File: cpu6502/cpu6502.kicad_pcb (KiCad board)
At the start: 2 copper layers, 140 x 100 mm, 34 parts, among them J1 Conn_01x02, J2 Conn_02x05_Odd_Even, J3 Conn_02x21_Odd_Even, U1 74LS161, U2 W65C02SxP / MC6802 / R6502, U3 74LS573, U4 74LS573, U5 74LS573, U6 74LS245, U7 ATF22V10C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

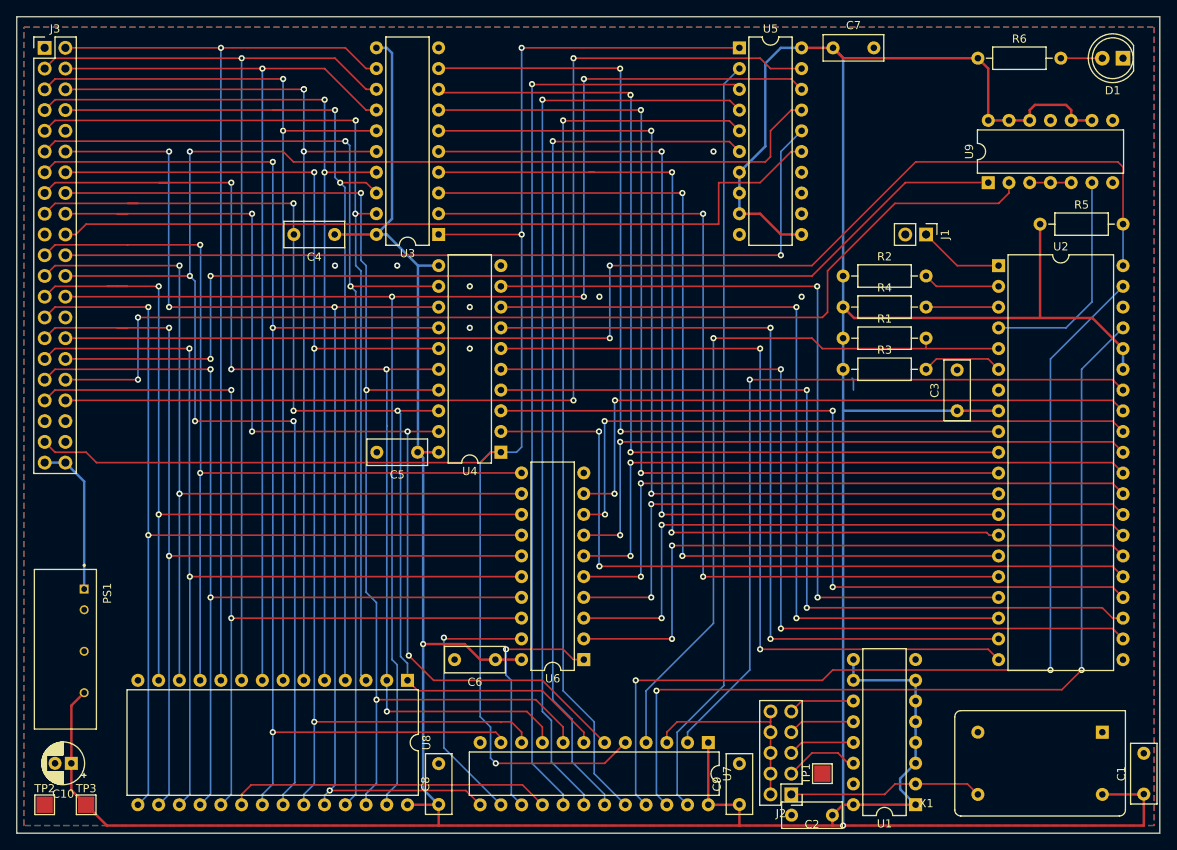
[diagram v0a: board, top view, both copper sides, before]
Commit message: Moved devices around and size reduced board.
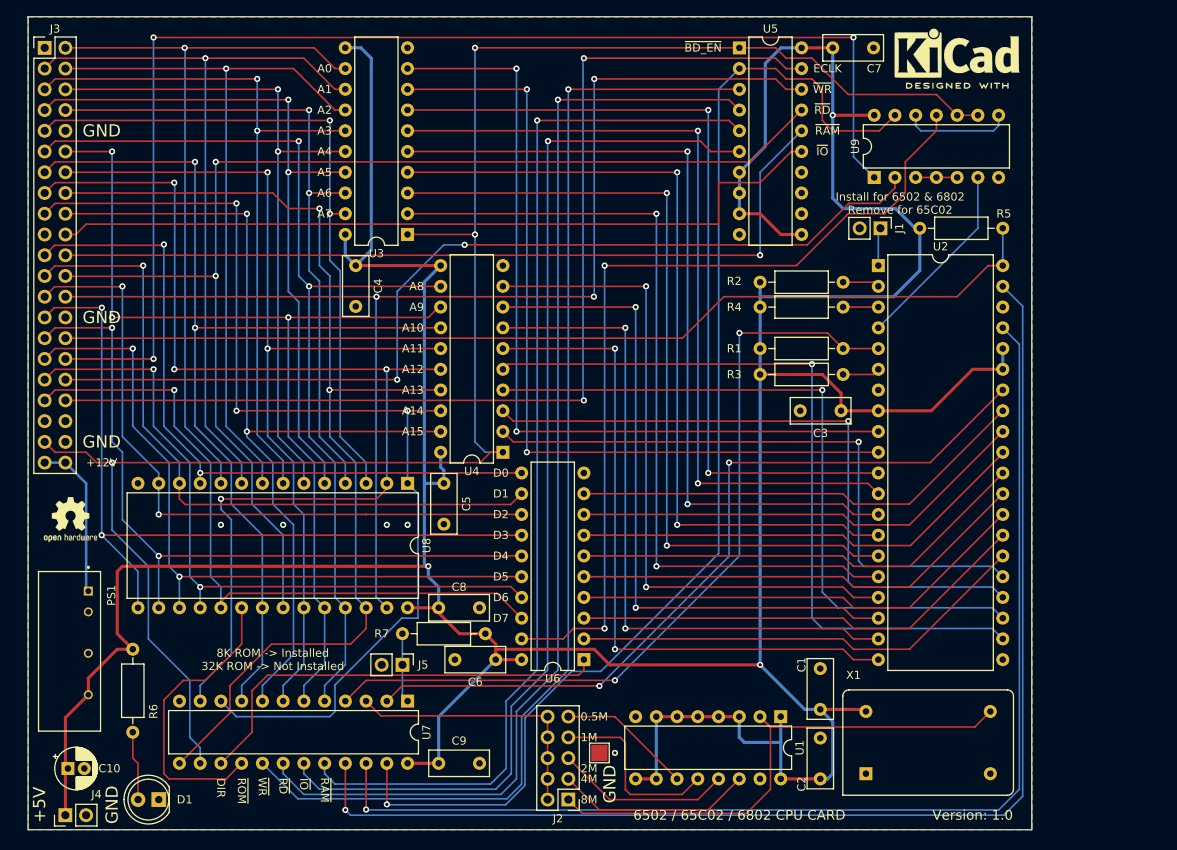
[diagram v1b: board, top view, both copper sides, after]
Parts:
- removed TP2, TP3: TestPoint, TestPoint:TestPoint_Pad_2.0x2.0mm
- added J4: Conn_01x02, Connector_PinHeader_2.54mm:PinHeader_1x02_P2.54mm_Vertical, F.Cu at (61.0, 148.6)
- added J5: Conn_01x02, Connector_PinHeader_2.54mm:PinHeader_1x02_P2.54mm_Vertical, F.Cu at (102.2, 130.2)
- added R7: 10.5K, Resistor_THT:R_Axial_DIN0207_L6.3mm_D2.5mm_P10.16mm_Horizontal, F.Cu at (102.2, 126.4)
- added REF**: OSHW-Logo2_7.3x6mm_SilkScreen, Symbol:OSHW-Logo2_7.3x6mm_SilkScreen, F.Cu at (61.6, 112.4)
- added REF**: KiCad-Logo2_6mm_SilkScreen, Symbol:KiCad-Logo2_6mm_SilkScreen, F.Cu at (170.2, 55.2)
- moved D1 149.0 mm to (72.4, 146.7)
- moved R6 126.3 mm to (69.2, 128.3), turned to -90 degrees
- moved C1 41.0 mm to (153.4, 135.6)
- moved U7 37.2 mm to (102.9, 134.6)
- moved C9 37.2 mm to (106.7, 142.2), turned to 0 degrees
- moved X1 29.4 mm to (159.0, 143.5), turned to 0 degrees
- moved TP1 27.4 mm to (126.4, 141.0), turned to 0 degrees
- moved J2 27.3 mm to (122.6, 146.7)
- moved U8 24.1 mm to (102.9, 108.0)
- moved C8 24.1 mm to (106.7, 123.2), turned to 0 degrees
- moved U1 19.7 mm to (148.6, 136.5), turned to -90 degrees
- moved R5 14.7 mm to (165.6, 76.7)
- moved U2 14.7 mm to (160.5, 81.3)
- moved C3 14.2 mm to (156.0, 99.1), turned to 180 degrees
- moved U9 14.0 mm to (160.0, 70.5)
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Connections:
- U7 pad 1: +5V -> /MEM_CONN/32Kn
- U7 pad 10: B_A11 -> B_A14
- U7 pad 11: B_A10 -> B_A12
- U7 pad 13: B_A9 -> B_A13
- U7 pad 14: ~{BUS_EN} -> ~{BD_EN}
- U7 pad 5: ~{BD_EN} -> B_A8
- U7 pad 6: B_A15 -> B_A9
- U7 pad 7: B_A14 -> B_A11
- U7 pad 8: B_A13 -> B_A15
- U7 pad 9: B_A12 -> B_A10
- U9 pad 10: +5V -> ~{BD_EN}
- U9 pad 11: unconnected-(U9-Pad11) -> ~{BUS_EN}
- U9 pad 12: +5V -> Net-(U9-Pad12)
- U9 pad 13: +5V -> ECLK
- U9 pad 8: unconnected-(U9-Pad8) -> Net-(U9-Pad12)
- U9 pad 9: +5V -> ~{BD_EN}
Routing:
- net +5V: track 581.6 -> 488.8 mm
- net ~{BUS_EN}: track 32.9 -> 106.8 mm, vias 1 -> 2
- net ECLK: track 93.9 -> 148.9 mm, vias 0 -> 1
- net /8M: track 23.9 -> 65.6 mm
- net B_A10: track 156.9 -> 119.3 mm, vias 3 -> 2
- net B_A11: track 150.9 -> 113.4 mm, vias 3 -> 2
- net ~{B_RD}: track 188.2 -> 150.9 mm, vias 4 -> 2
- net CLK_39: track 117.8 -> 153.4 mm, vias 2 -> 1
- net ~{RESET}: track 156.0 -> 123.1 mm, vias 2 -> 0
- net CLK_37: track 111.6 -> 144.1 mm, vias 2 -> 1
- net B_D4: track 119.2 -> 89.9 mm
- net B_A9: track 145.5 -> 116.4 mm, vias 4 -> 3
- net B_D5: track 115.3 -> 87.3 mm
- net B_A6: track 109.6 -> 81.8 mm
- net B_D6: track 112.8 -> 85.4 mm
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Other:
- board size 140 x 100 mm -> 122.9 x 99.6 mm
- board text added: "+12V"
- board text added: "+5V"
- board text added: "0.5M"
- board text added: "1M"
- board text added: "2M"
- board text added: "4M"
- board text added: "6502 / 65C02 / 6802 CPU CARD"
- board text added: "8K ROM -> Installed 32K ROM -> Not Installed"
- board text added: "8M"
- board text added: "A0"
- board text added: "A1"
- board text added: "A10"
- board text added: "A11"
- board text added: "A12"
- board text added: "A13"
- board text added: "A14"
- board text added: "A15"
- board text added: "A2"
- board text added: "A3"
- board text added: "A4"
- board text added: "A5"
- board text added: "A6"
- board text added: "A7"
- board text added: "A8"
- board text added: "A9"
- board text added: "D0"
- board text added: "D1"
- board text added: "D2"
- board text added: "D3"
- board text added: "D4"
- board text added: "D5"
- board text added: "D6"
- board text added: "D7"
- board text added: "DIR"
- board text added: "ECLK"
- board text added: "GND"
- board text added: "Install for 6502 & 6802 Remove for 65C02"
- board text added: "Version: 1.0"
- board text added: "~{BD_EN}"
- board text added: "~{IO}"
- board text added: "~{RAM}"
- board text added: "~{RD}"
- board text added: "~{ROM}"
- board text added: "~{WR}"

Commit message: Updated to as built.
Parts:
- C10: value 10 uF -> 47 uF
- R6: value 1K -> 3.3K
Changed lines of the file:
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@@
       (effects (font (size 1 1) (thickness 0.15)))
     )
-    (fp_text value "1K" (at 5.08 2.37 90) (layer "F.Fab")
+    (fp_text value "3.3K" (at 5.08 2.37 90) (layer "F.Fab")
       (effects (font (size 1 1) (thickness 0.15)))
     )
@@
       (effects (font (size 1 1) (thickness 0.15)))
     )
-    (fp_text value "10 uF" (at 1 3.75) (layer "F.Fab")
-      (effects (font (size 1 1) (thickness 0.15)))
-    )
+    (fp_text value "47 uF" (at 1 3.75) (layer "F.Fab")
+      (effects (font (size 1 1) (thickness 0.15)))
+    )
